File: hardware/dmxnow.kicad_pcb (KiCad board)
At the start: 2 copper layers, 146 x 54 mm, 59 parts, among them J1 WAGO 2604-1102 (L N in), J2 DMX tail (1 GND 2 B 3 A), J3 PROG (3V3 GND D- D+ EN BOOT), J4 WAGO 2604-1102 (L_SW N out 1), J5 WAGO 2604-1102 (VLED_IN GND_L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, J6 WAGO 2604-1105 (VLED CH1-CH4), J7 WAGO 2604-1102 (L_SW N out 2,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, K1 G5RL-U1A-E DC5, Q1 AO3400A, Q2 AOD4184A, Q3 AOD4184A, Q4 AOD4184A, Q5 AOD4184A, SW1 PTS810 (BOOT/maintenance), U1 ESP32-C3-MINI-1-N4, U2 SP3485EN, U3 AP2112K-3.3, U4 74AHCT125

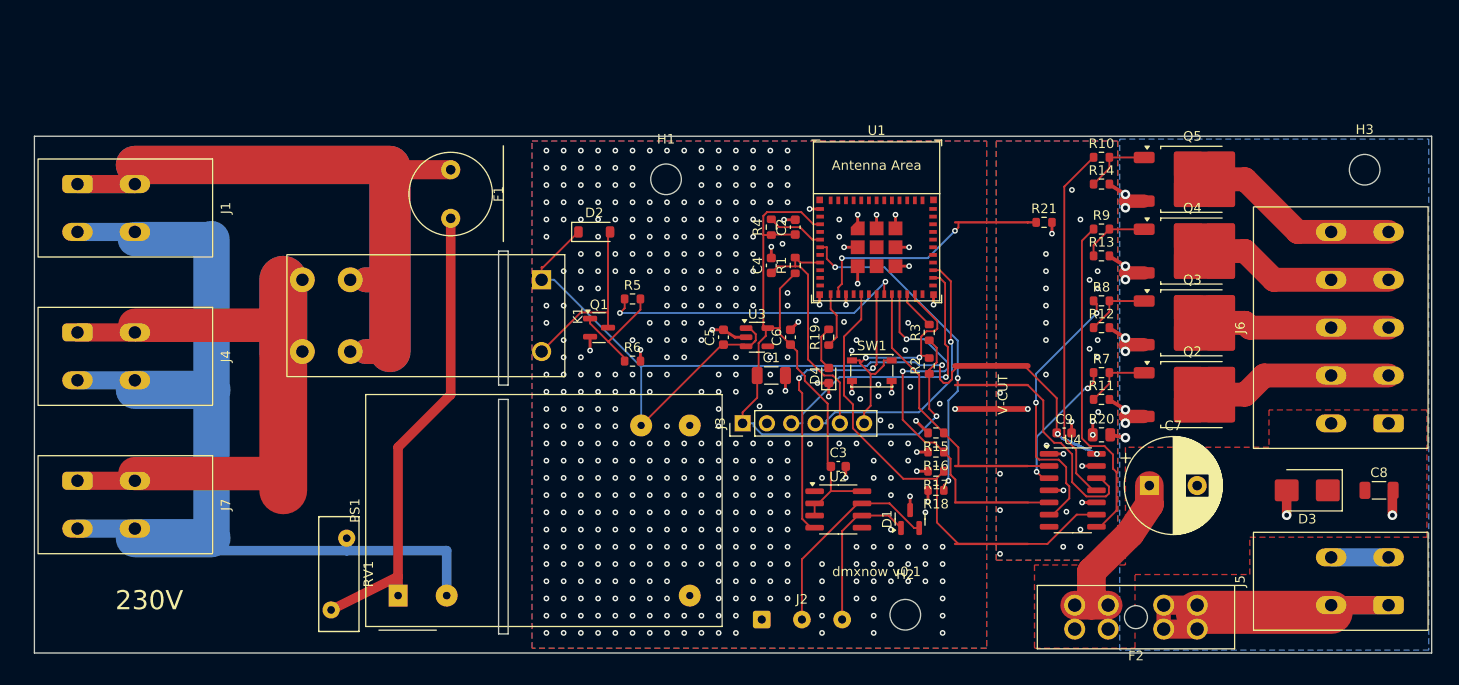
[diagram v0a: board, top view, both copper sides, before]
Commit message: hardware: relais G5RL-1A-E-HR, cotes WAGO 2604 et IRM-03 vérifiées sur fiches
- K1 : G5RL-U1A-E (bistable, incompatible avec la commande MOSFET) remplacé par
  G5RL-1A-E-HR DC5 (LCSC C113250), même implantation ; corps 29,0 x 12,7 mm.
- WAGO 2604 : rangées de broches à 8,2 mm (au lieu de 6), corps 16,3 mm + levier
  2,9 mm, largeur (n-1) x 5 + 7,4 mm, pastilles 1,9 x 2,8 mm.
- Placement : J1/J4/J7 décalés de 0,7 mm vers le bord (3 mm entre le bus N et les
  pastilles L_SW), J6 et canaux de 0,5 mm, H3 de 0,5 mm (chevauchement de courtyard).
- PS1 : empreinte KiCad IRM-03 conforme à la fiche Mean Well 2025-08-08.
- Références LCSC ajoutées (K1, WAGO 2604-1102, IRM-03-5).
- SPEC (4.5, V-HW-03/04/09/10), ADR 0005 amendé, REVIEW.md, index des fiches.

Co-Authored-By: Claude Opus 5.5 <noreply@anthropic.com>
Claude-Session: https://claude.ai/code/session_01B51M6ZY5abLxTmcevvc8Le
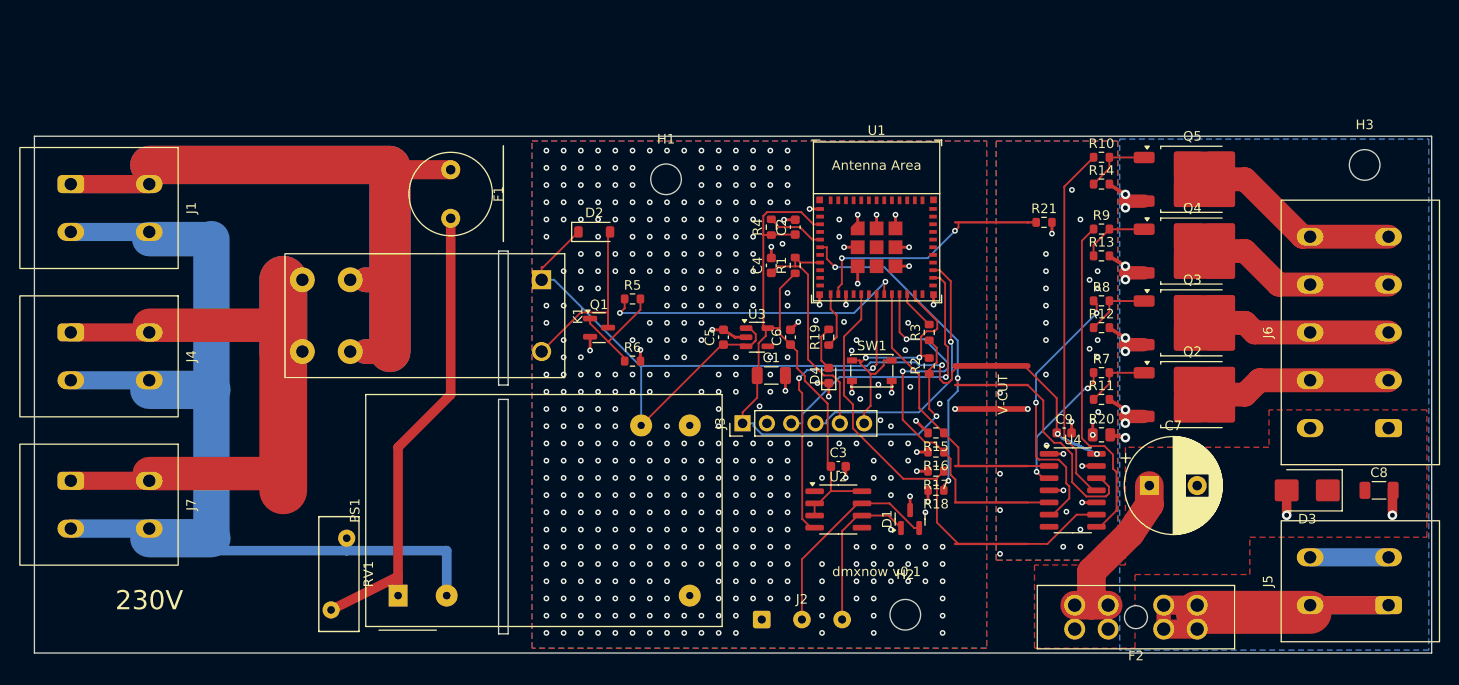
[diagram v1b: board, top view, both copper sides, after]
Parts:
- K1: value G5RL-U1A-E DC5 -> G5RL-1A-E-HR DC5; footprint dmxnow:Relay_SPST_Omron_G5RL-U1A-E -> dmxnow:Relay_SPST_Omron_G5RL-1A-E-HR
- moved J1 0.70 mm to (53.8, 55.0)
- moved J4 0.70 mm to (53.8, 70.5)
- moved J7 0.70 mm to (53.8, 86.0)
- moved H3 0.50 mm to (189.0, 53.0)
- moved J6 0.50 mm to (191.5, 80.5)
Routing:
- net VLED_IN: track 35.5 -> 37.7 mm
- net GND_LED: track 28.8 -> 31.0 mm
- net N: track 103.8 -> 105.9 mm
- net L_SW: track 76.5 -> 77.9 mm
- net L_IN: track 124.5 -> 125.9 mm

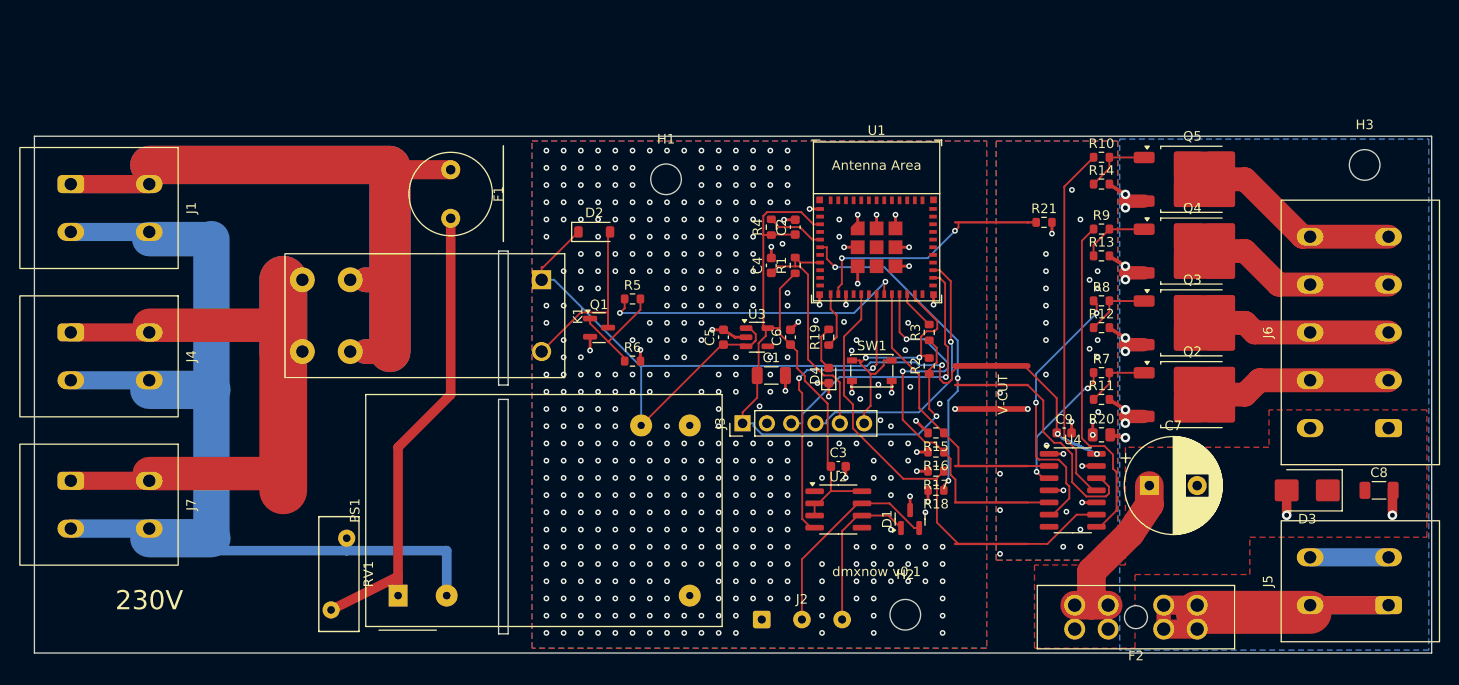
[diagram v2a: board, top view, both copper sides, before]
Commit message: hardware: rév. 0.3 après revue de conception (3 relecteurs indépendants)
Bloquants corrigés :
- V-cut remplacé par une fente fraisée + 3 languettes perforées : la rainure
  V aurait coupé en fabrication les 7 pistes qui traversent la découpe, et
  JLCPCB refuse le V-cut sous 70 x 70 mm (ADR 0007 amendé).
- Fichiers de placement convertis aux conventions JLCPCB (SOT-23, SOT-23-5,
  SOIC, TO-252, ESP32-C3-MINI-1, centres des traversants) ; variantes BOM/CPL
  « full » (CMS + traversants) et « smt ».
- F1 : fusible céramique 5x20 T500mA H (1500 A) dans un support Schurter
  0031.8201, placé dans une bande de 10 mm ajoutée au-dessus de la zone 230 V.
- R15-R18 4,7k : GPIO6 (PWM1) a un pull-up interne ~45k au reset, le canal 1
  s'allumait au démarrage.

Autres corrections :
- Vias 0,9/0,35 mm (anneau >= 0,254 mm exigé en 2 oz), perçage WAGO 1,4 mm.
- Aucun via dans une pastille CMS (Freerouting via_at_smd off, routeur de
  finition, nouveau contrôle dans check.py).
- MOSFET AOD2610E 60 V (R-10 clos), C7 Nichicon UHW 2 A d'ondulation.
- Cuivre 230 V élargi (bus N 7,1 mm, doigts L_SW 7,4 mm), 3 vias par source.
- R22 pull-up DMX_TX, C10 47 uF sur +5V, R23 pull-up BOARD_SENSE, R19 100R.
- Zone interdite de 7,2 mm autour de la broche NC de PS1 (rangée AC).
- Règle DRC d'exception limitée aux pastilles de K1 et PS1.
- Plans LED avec pastilles traversantes en réserves thermiques, marquage
  de polarité de J5, via de masse pré-placés sur les pastilles isolées.
- SPEC, REVIEW.md et README mis à jour.

Co-Authored-By: Claude Opus 5.5 <noreply@anthropic.com>
Claude-Session: https://claude.ai/code/session_01B51M6ZY5abLxTmcevvc8Le
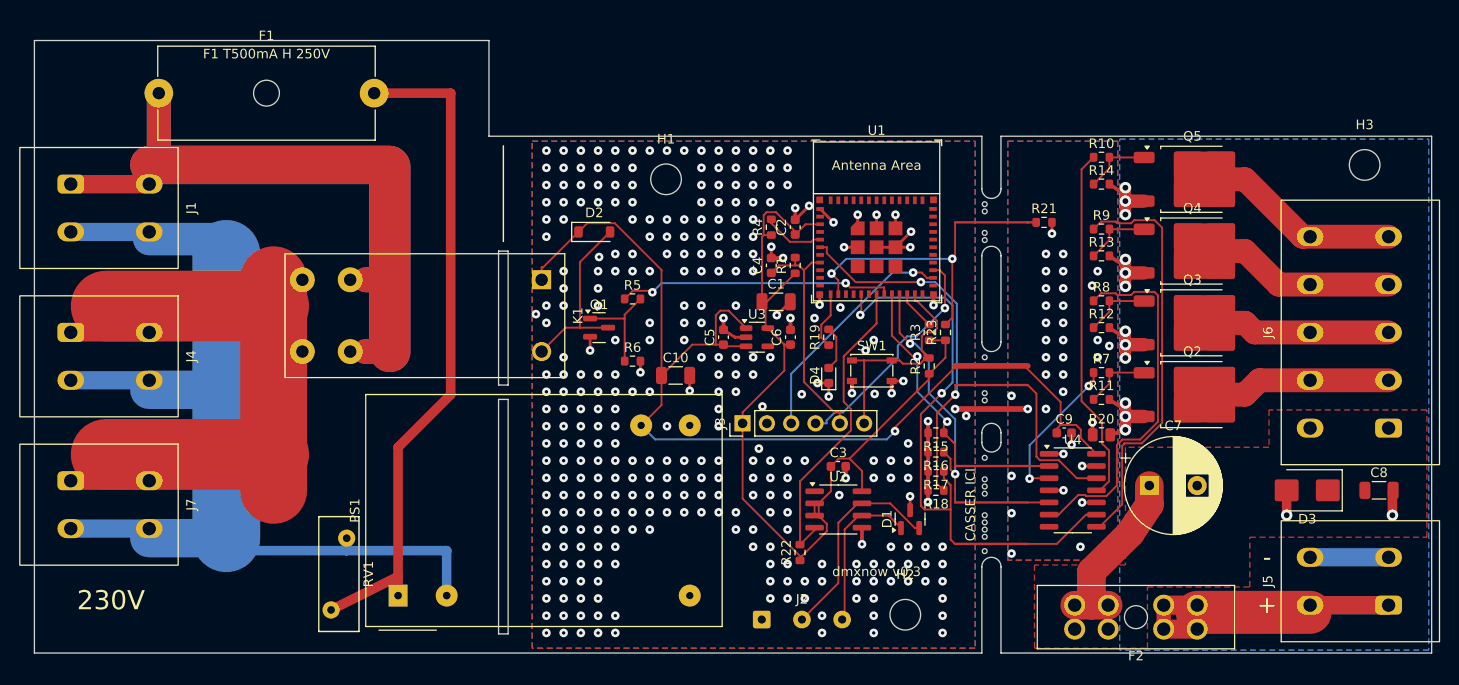
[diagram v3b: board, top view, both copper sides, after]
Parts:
- added C10: 47uF 10V, Capacitor_SMD:C_1206_3216Metric, F.Cu at (117.0, 75.0)
- added MB: , , F.Cu at (149.3, 85.8)
- added MB: , , F.Cu at (149.3, 83.6)
- added MB: , , F.Cu at (149.3, 87.3)
- added MB: , , F.Cu at (149.3, 86.6)
- added MB: , , F.Cu at (149.3, 91.1)
- added MB: , , F.Cu at (149.3, 91.8)
- added MB: , , F.Cu at (149.3, 93.3)
- added MB: , , F.Cu at (149.3, 89.6)
- added MB: , , F.Cu at (149.3, 60.1)
- added MB: , , F.Cu at (149.3, 73.1)
- added MB: , , F.Cu at (149.3, 77.6)
- added MB: , , F.Cu at (149.3, 60.9)
- added MB: , , F.Cu at (149.3, 57.1)
- added MB: , , F.Cu at (149.3, 90.3)
- added MB: , , F.Cu at (149.3, 76.8)
- added MB: , , F.Cu at (149.3, 57.9)
- added R22: 10k, Resistor_SMD:R_0603_1608Metric, F.Cu at (130.0, 93.5)
- added R23: 100k, Resistor_SMD:R_0603_1608Metric, F.Cu at (145.2, 70.5)
- C4, C5, C6: value 1uF 16V -> 1uF
- F1: value TR5 T500mA 250V -> 5x20 holder, T500mA H; footprint Fuse:Fuse_Littelfuse_372_D8.50mm -> Fuse:Fuseholder_Cylinder-5x20mm_Schurter_0031_8201_Horizontal_Open
- Q2, Q3, Q4, Q5: value AOD4184A -> AOD2610E
- R15, R16, R17, R18: value 100k -> 4.7k
- R19: value 1k -> 100R
- moved F1 31.5 mm to (63.0, 45.5), turned to 0 degrees
- moved C1 7.72 mm to (127.5, 67.3)
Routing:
- net L_PSU: track 49.5 -> 70.6 mm
- net GND: track 56.5 -> 69.1 mm, vias 464 -> 359
- net PWM3: track 51.0 -> 62.7 mm, vias 0 -> 2
- net GND_LED: track 31.0 -> 42.2 mm, vias 11 -> 14
- net DRV2: track 28.9 -> 38.6 mm, vias 2 -> 0
- net BOARD_SENSE: track 26.4 -> 35.3 mm
- net +5V: track 102.5 -> 111.1 mm, vias 3 -> 1
- net L_IN: track 125.9 -> 134.5 mm
- net DRV3: track 35.1 -> 43.4 mm
- net USB_DM: track 30.2 -> 24.6 mm
- net PWM2: track 42.1 -> 37.1 mm
- net USB_DP: track 29.0 -> 24.3 mm
- net +3V3: track 97.2 -> 92.8 mm, vias 1 -> 0
- net BOOT: track 27.6 -> 24.1 mm, vias 2 -> 0
- net RELAY_CTRL: track 32.1 -> 28.8 mm
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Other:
- board size 146 x 54 mm -> 146 x 64 mm
- board text added: "+"
- board text added: "-"
- board text added: "CASSER ICI"
- board text added: "F1 T500mA H 250V"
- board text added: "dmxnow v0.3"
- board text removed: "V-CUT"
- board text removed: "dmxnow v0.1"

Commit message: hardware: seconde passe de revue (rév. 0.3b)
Corrections issues de la seconde revue indépendante :
- CPL : Q2-Q5 (AOD2610E, C282428) tournés de 180° (empreinte JLC : languette
  à gauche) ; centres des WAGO 2604 = centre du réseau de broches.
- Broche NC de PS1 : règle DRC ps1_nc_pin (6 mm depuis le bord de la
  pastille), zone interdite agrandie, J2 décalé de 1 mm.
- DRC canary (gen/drc_canary.py, make check et CI KiCad 9) : des défauts
  injectés doivent déclencher chaque règle 230 V personnalisée.
- insideCourtyard -> intersectsCourtyard (KiCad 7 à 9).
- Languette B raccourcie et mieux perforée, vias OE de U4 et de R20 à
  >= 0,25 mm des pastilles, col VLED élargi, RV1 décalé de PS1.

Routage :
- Face arrière réservée au plan de masse (coût de routage 3-4x en B.Cu) ;
  via de masse pré-placé pour chaque pastille CMS de masse ; optimiseur
  Freerouting limité à 8 passes.
- Routeur de finition : contour et fentes pris comme obstacles, jonction des
  îlots de masse, distance segment-segment exacte, aucun via sur sa propre
  pastille, marge au bord de carte, suppression des segments de longueur nulle.

Contrôles : netlist 0 erreur, PCB 0 erreur, DRC 0 erreur / 0 non connecté,
canari OK.

Co-Authored-By: Claude Opus 5.5 <noreply@anthropic.com>
Claude-Session: https://claude.ai/code/session_01B51M6ZY5abLxTmcevvc8Le
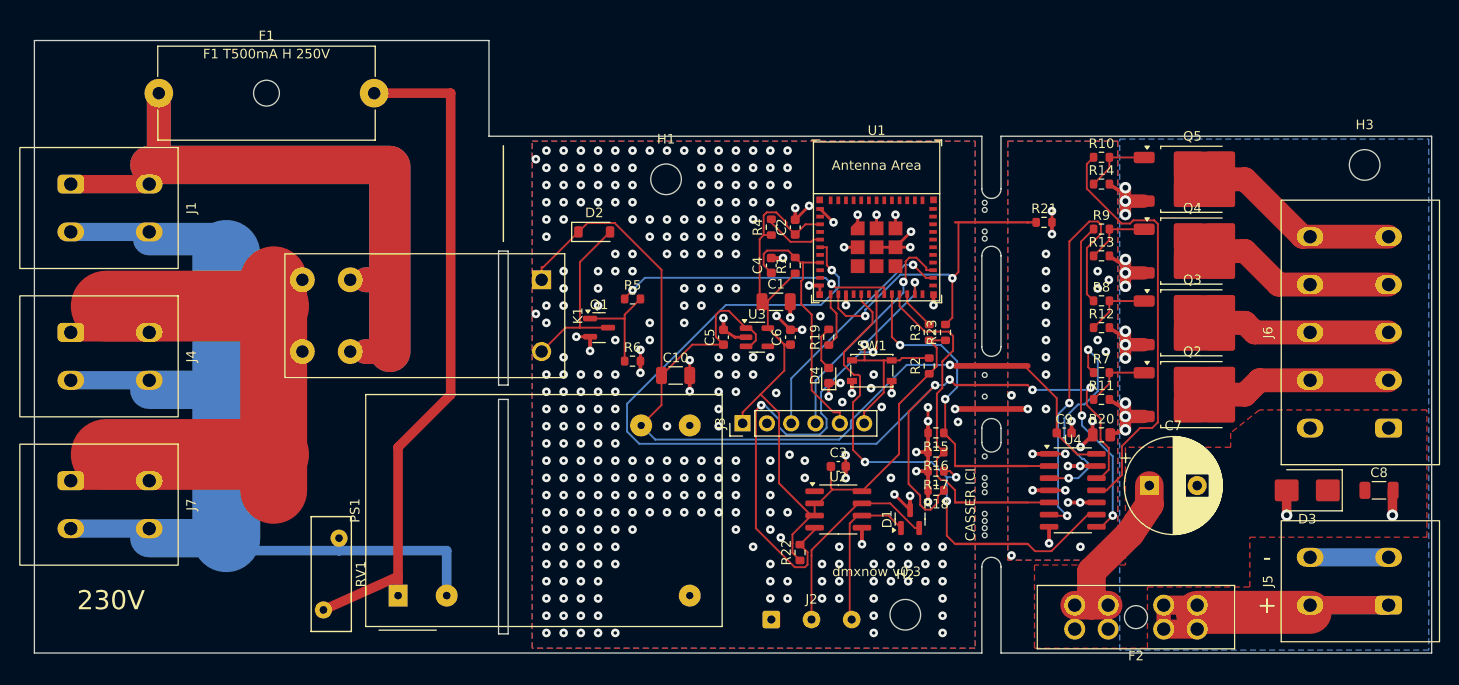
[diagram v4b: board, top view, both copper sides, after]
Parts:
- removed the MB at (149.3, 85.8)
- removed the MB at (149.3, 83.6)
- removed the MB at (149.3, 87.3)
- removed the MB at (149.3, 86.6)
- removed the MB at (149.3, 91.1)
- removed the MB at (149.3, 91.8)
- removed the MB at (149.3, 93.3)
- removed the MB at (149.3, 89.6)
- removed the MB at (149.3, 60.1)
- removed the MB at (149.3, 73.1)
- removed the MB at (149.3, 77.6)
- removed the MB at (149.3, 60.9)
- removed the MB at (149.3, 57.1)
- removed the MB at (149.3, 90.3)
- removed the MB at (149.3, 76.8)
- removed the MB at (149.3, 57.9)
- added MB: , , F.Cu at (149.3, 57.0)
- added MB: , , F.Cu at (149.3, 75.0)
- added MB: , , F.Cu at (149.3, 89.5)
- added MB: , , F.Cu at (149.3, 91.0)
- added MB: , , F.Cu at (149.3, 86.5)
- added MB: , , F.Cu at (149.3, 60.0)
- added MB: , , F.Cu at (149.3, 60.7)
- added MB: , , F.Cu at (149.3, 91.7)
- added MB: , , F.Cu at (149.3, 87.2)
- added MB: , , F.Cu at (149.3, 90.2)
- added MB: , , F.Cu at (149.3, 57.7)
- added MB: , , F.Cu at (149.3, 83.5)
- added MB: , , F.Cu at (149.3, 77.2)
- added MB: , , F.Cu at (149.3, 85.7)
- moved J2 1.00 mm to (127.0, 100.5)
- moved RV1 0.80 mm to (80.2, 99.5)
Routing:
- net PWM4: track 61.4 -> 117.1 mm, vias 2 -> 5
- net GND: track 69.1 -> 98.8 mm, vias 359 -> 337
- net DMX_TX: track 32.5 -> 51.3 mm, vias 0 -> 2
- net DRV3: track 43.4 -> 34.0 mm, vias 0 -> 2
- net DRV4: track 37.3 -> 44.7 mm
- net DRV1: track 15.9 -> 22.8 mm
- net DRV2: track 38.6 -> 44.7 mm, vias 0 -> 2
- net PWM3: track 62.7 -> 56.8 mm, vias 2 -> 3
- net PWM1: track 31.1 -> 35.1 mm
- net EN: track 24.7 -> 27.8 mm
- net BOOT: track 24.1 -> 27.2 mm, vias 0 -> 2
- net +3V3: track 92.8 -> 89.8 mm
- net L_PSU: track 70.6 -> 71.3 mm
- net PWM2: track 37.1 -> 37.7 mm, vias 2 -> 0
- net +5V: track 111.1 -> 111.7 mm
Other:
- outline, holes or cut-outs redrawn
